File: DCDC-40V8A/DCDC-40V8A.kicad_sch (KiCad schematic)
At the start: 0 parts

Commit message: wip
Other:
- added sheet ADC-Coprocessor (adc_coprocessor.kicad_sch)
- sheet Power ports: added EN; removed none
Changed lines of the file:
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@@
 	(generator_version "9.0")
 	(paper "A4")
+	(junction
+		(at 104.14 52.07)
+		(diameter 0)
+		(color 0 0 0 0)
+	)
 	(bus
 		(pts
-			(xy 88.9 52.07) (xy 118.11 52.07)
+			(xy 88.9 52.07) (xy 104.14 52.07)
+		)
+		(stroke
+			(width 0)
+			(type default)
+		)
+	)
+	(bus
+		(pts
+			(xy 104.14 52.07) (xy 118.11 52.07)
 		)
 		(stroke
@@
 		(pts
 			(xy 88.9 54.61) (xy 118.11 54.61)
+		)
+		(stroke
+			(width 0)
+			(type default)
+		)
+	)
+	(bus
+		(pts
+			(xy 104.14 52.07) (xy 104.14 120.65)
 		)
 		(stroke
@@
 	)
 	(sheet
-		(at 118.11 30.48)
-		(size 48.26 106.68)
+		(at 49.53 120.65)
+		(size 118.11 31.75)
 		(exclude_from_sim no)
 		(in_bom yes)
@@
 			(color 0 0 0 0.0000)
 		)
+		(property "Sheetname" "ADC-Coprocessor"
+			(at 49.53 119.9384 0)
+			(effects
+				(font
+					(size 1.27 1.27)
+				)
+				(justify left bottom)
+			)
+		)
+		(property "Sheetfile" "adc_coprocessor.kicad_sch"
+			(at 49.53 152.9846 0)
+			(effects
+				(font
+					(size 1.27 1.27)
+				)
+				(justify left top)
+			)
+		)
+		(pin "I2C" bidirectional
+			(at 104.14 120.65 90)
+			(effects
+				(font
+					(size 1.27 1.27)
+				)
+				(justify right)
+			)
+		)
+		(instances
+			(project "DCDC-40V8A"
+				(path "/c2f330be-6ca8-4ed0-86db-c2e1bfb68425"
+					(page "4")
+				)
+			)
+		)
+	)
+	(sheet
+		(at 118.11 30.48)
+		(size 48.26 69.85)
+		(exclude_from_sim no)
+		(in_bom yes)
+		(on_board yes)
+		(dnp no)
+		(fields_autoplaced yes)
+		(stroke
+			(width 0.1524)
+			(type solid)
+		)
+		(fill
+			(color 0 0 0 0.0000)
+		)
 		(property "Sheetname" "Control-Connector"
 			(at 118.11 29.7684 0)
@@
 		)
 		(property "Sheetfile" "control_connector.kicad_sch"
-			(at 118.11 137.7446 0)
+			(at 118.11 100.9146 0)
 			(effects
 				(font
@@
 		)
 		(pin "Left_RX" input
-			(at 118.11 110.49 180)
+			(at 118.11 91.44 180)
 			(effects
 				(font
@@
 		)
 		(pin "Left_TX" output
-			(at 118.11 113.03 180)
+			(at 118.11 93.98 180)
 			(effects
 				(font
@@
 		)
 		(pin "Right_RX" input
-			(at 166.37 113.03 0)
+			(at 166.37 93.98 0)
 			(effects
 				(font
@@
 		)
 		(pin "Right_TX" output
-			(at 166.37 110.49 0)
+			(at 166.37 91.44 0)
 			(effects
 				(font
@@
 			)
 		)
+		(pin "EN" input
+			(at 76.2 99.06 270)
+			(effects
+				(font
+					(size 1.27 1.27)
+				)
+				(justify left)
+			)
+		)

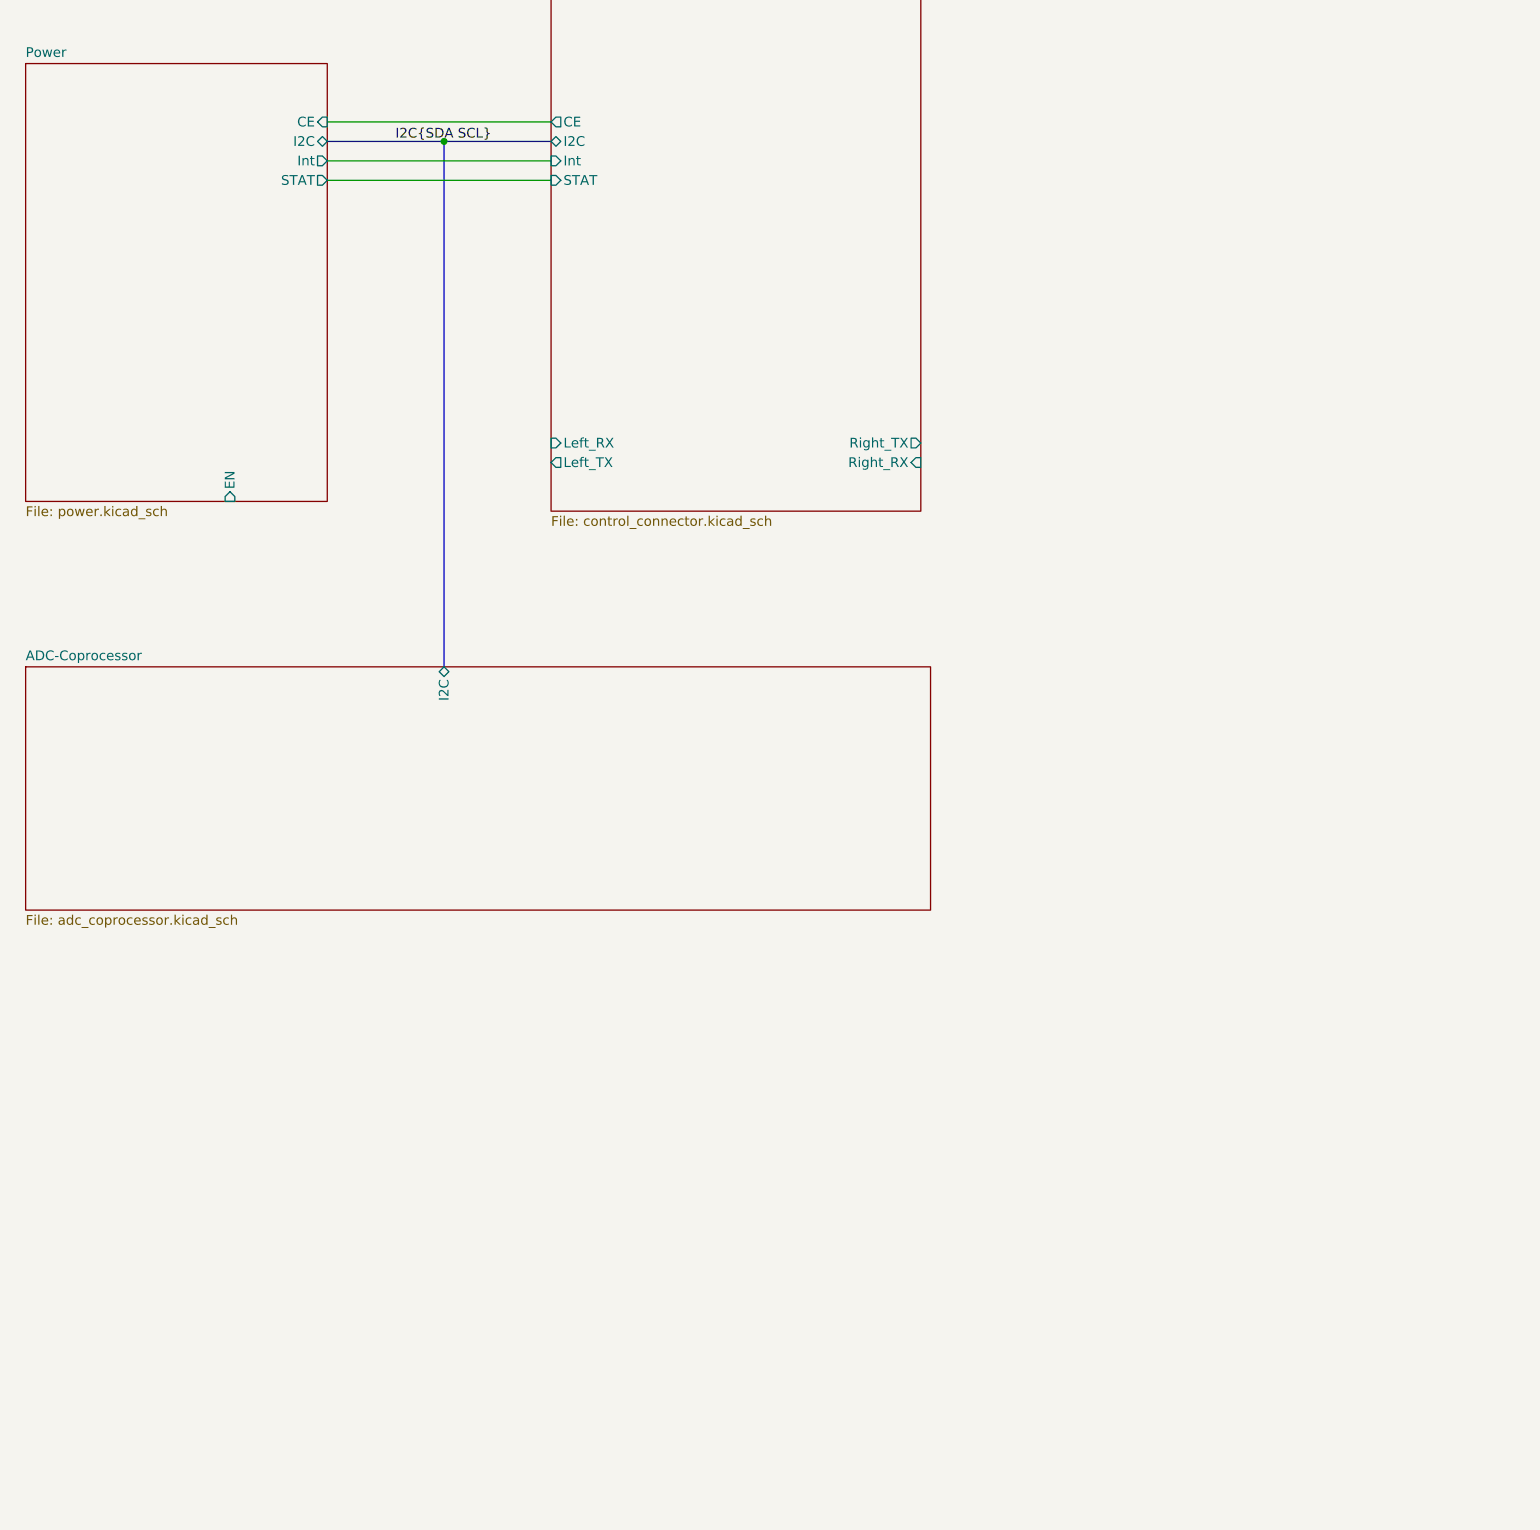
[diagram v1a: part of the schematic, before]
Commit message: move adc MUX and discharge to new sheet
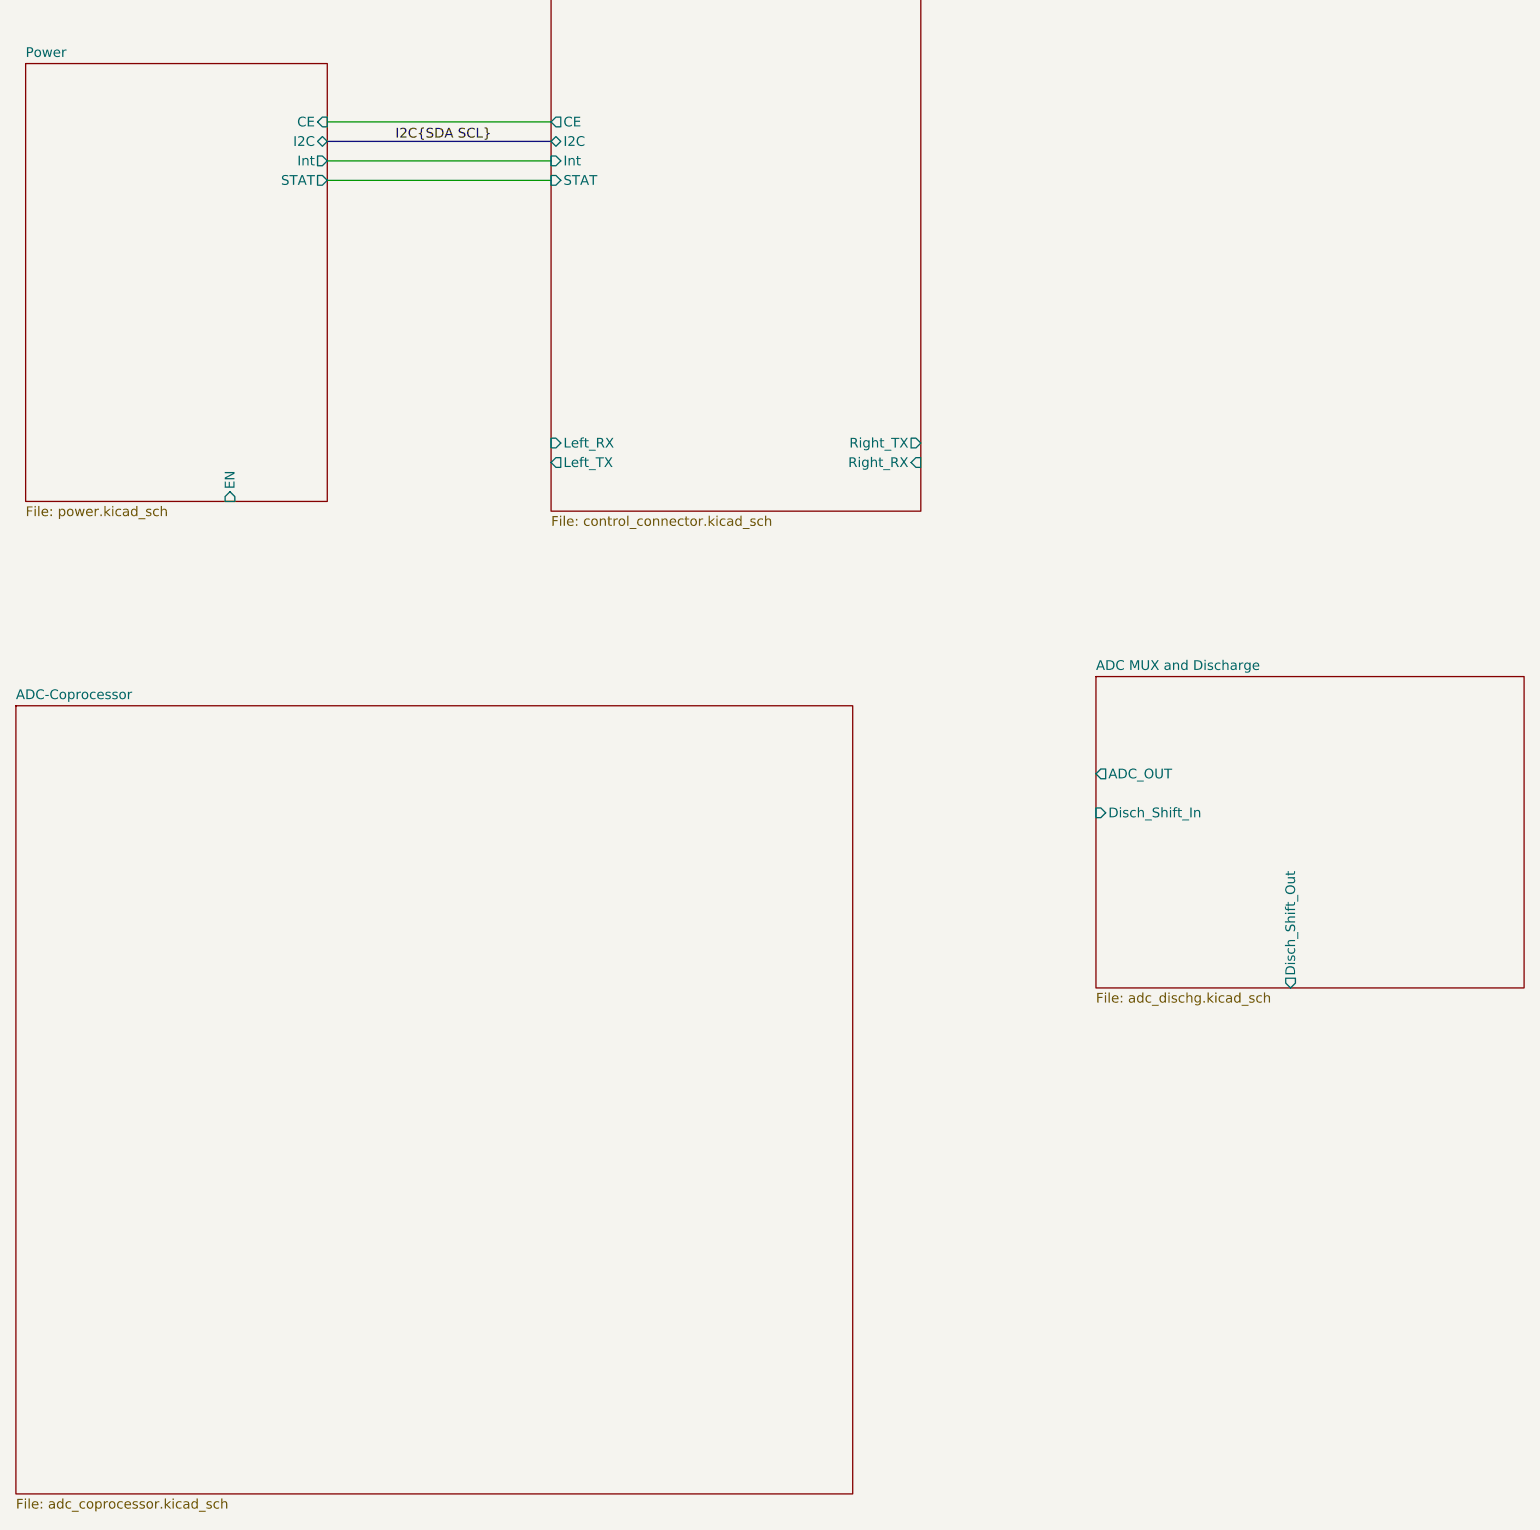
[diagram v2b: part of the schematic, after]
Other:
- added sheet ADC MUX and Discharge (adc_dischg.kicad_sch)
- sheet ADC-Coprocessor ports: added none; removed I2C
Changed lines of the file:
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@@
 (kicad_sch
-	(version 20250114)
+	(version 20260306)
 	(generator "eeschema")
-	(generator_version "9.0")
-	(paper "A4")
-	(junction
-		(at 104.14 52.07)
-		(diameter 0)
-		(color 0 0 0 0)
-	)
+	(generator_version "10.0")
+	(paper "A3")
 	(bus
 		(pts
-			(xy 88.9 52.07) (xy 104.14 52.07)
-		)
-		(stroke
-			(width 0)
-			(type default)
-		)
-	)
-	(bus
-		(pts
-			(xy 104.14 52.07) (xy 118.11 52.07)
+			(xy 88.9 52.07) (xy 118.11 52.07)
 		)
 		(stroke
@@
 		(pts
 			(xy 88.9 54.61) (xy 118.11 54.61)
-		)
-		(stroke
-			(width 0)
-			(type default)
-		)
-	)
-	(bus
-		(pts
-			(xy 104.14 52.07) (xy 104.14 120.65)
 		)
 		(stroke
@@
 	)
 	(sheet
-		(at 49.53 120.65)
-		(size 118.11 31.75)
+		(at 48.26 125.73)
+		(size 109.22 102.87)
 		(exclude_from_sim no)
 		(in_bom yes)
@@
 		)
 		(fill
-			(color 0 0 0 0.0000)
+			(color 0 0 0 0)
 		)
 		(property "Sheetname" "ADC-Coprocessor"
-			(at 49.53 119.9384 0)
+			(at 48.26 125.0184 0)
+			(show_name no)
+			(do_not_autoplace no)
 			(effects
 				(font
@@
 		)
 		(property "Sheetfile" "adc_coprocessor.kicad_sch"
-			(at 49.53 152.9846 0)
+			(at 48.26 229.1846 0)
+			(show_name no)
+			(do_not_autoplace no)
 			(effects
 				(font
@@
 				)
 				(justify left top)
-			)
-		)
-		(pin "I2C" bidirectional
-			(at 104.14 120.65 90)
-			(effects
-				(font
-					(size 1.27 1.27)
-				)
-				(justify right)
 			)
 		)
@@
 				(path "/c2f330be-6ca8-4ed0-86db-c2e1bfb68425"
 					(page "4")
+				)
+			)
+		)
+	)
+	(sheet
+		(at 189.23 121.92)
+		(size 55.88 40.64)
+		(exclude_from_sim no)
+		(in_bom yes)
+		(on_board yes)
+		(dnp no)
+		(fields_autoplaced yes)
+		(stroke
+			(width 0.1524)
+			(type solid)
+		)
+		(fill
+			(color 0 0 0 0)
+		)
+		(property "Sheetname" "ADC MUX and Discharge"
+			(at 189.23 121.2084 0)
+			(show_name no)
+			(do_not_autoplace no)
+			(effects
+				(font
+					(size 1.27 1.27)
+				)
+				(justify left bottom)
+			)
+		)
+		(property "Sheetfile" "adc_dischg.kicad_sch"
+			(at 189.23 163.1446 0)
+			(show_name no)
+			(do_not_autoplace no)
+			(effects
+				(font
+					(size 1.27 1.27)
+				)
+				(justify left top)
+			)
+		)
+		(pin "ADC_OUT" output
+			(at 189.23 134.62 180)
+			(effects
+				(font
+					(size 1.27 1.27)
+				)
+				(justify left)
+			)
+		)
+		(pin "Disch_Shift_In" input
+			(at 189.23 139.7 180)
+			(effects
+				(font
+					(size 1.27 1.27)
+				)
+				(justify left)
+			)
+		)
+		(pin "Disch_Shift_Out" output
+			(at 214.63 162.56 270)
+			(effects
+				(font
+					(size 1.27 1.27)
+				)
+				(justify left)
+			)
+		)
+		(instances
+			(project "DCDC-40V8A"
+				(path "/c2f330be-6ca8-4ed0-86db-c2e1bfb68425"
+					(page "6")
 				)
 			)
@@
 		)
 		(fill
-			(color 0 0 0 0.0000)
+			(color 0 0 0 0)
 		)
 		(property "Sheetname" "Control-Connector"
 			(at 118.11 29.7684 0)
+			(show_name no)
+			(do_not_autoplace no)
 			(effects
 				(font
@@
 		(property "Sheetfile" "control_connector.kicad_sch"
 			(at 118.11 100.9146 0)
+			(show_name no)
+			(do_not_autoplace no)
 			(effects
 				(font
@@
 		)
 		(fill
-			(color 0 0 0 0.0000)
+			(color 0 0 0 0)
 		)
 		(property "Sheetname" "Power"
 			(at 49.53 41.1984 0)
+			(show_name no)
+			(do_not_autoplace no)
 			(effects
 				(font
@@
 		(property "Sheetfile" "power.kicad_sch"
 			(at 49.53 99.6446 0)
-			(effects
-				(font
+			(show_name no)
+			(do_not_autoplace no)
+			(effects
+				(font

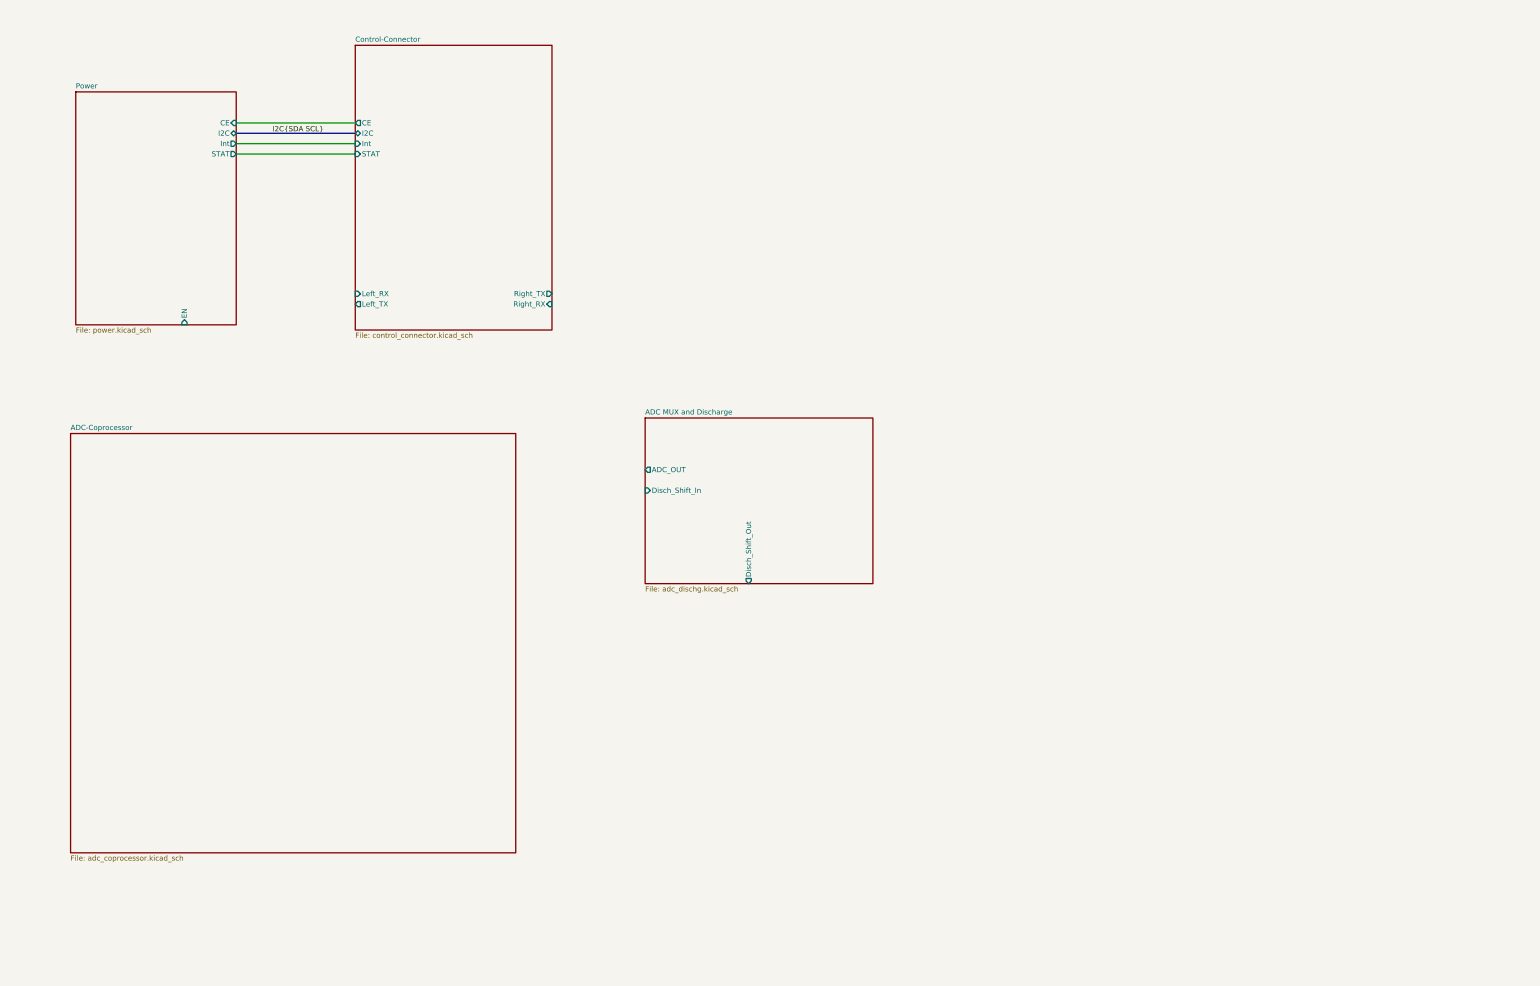
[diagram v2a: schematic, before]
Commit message: added discharge circuitry and help texts
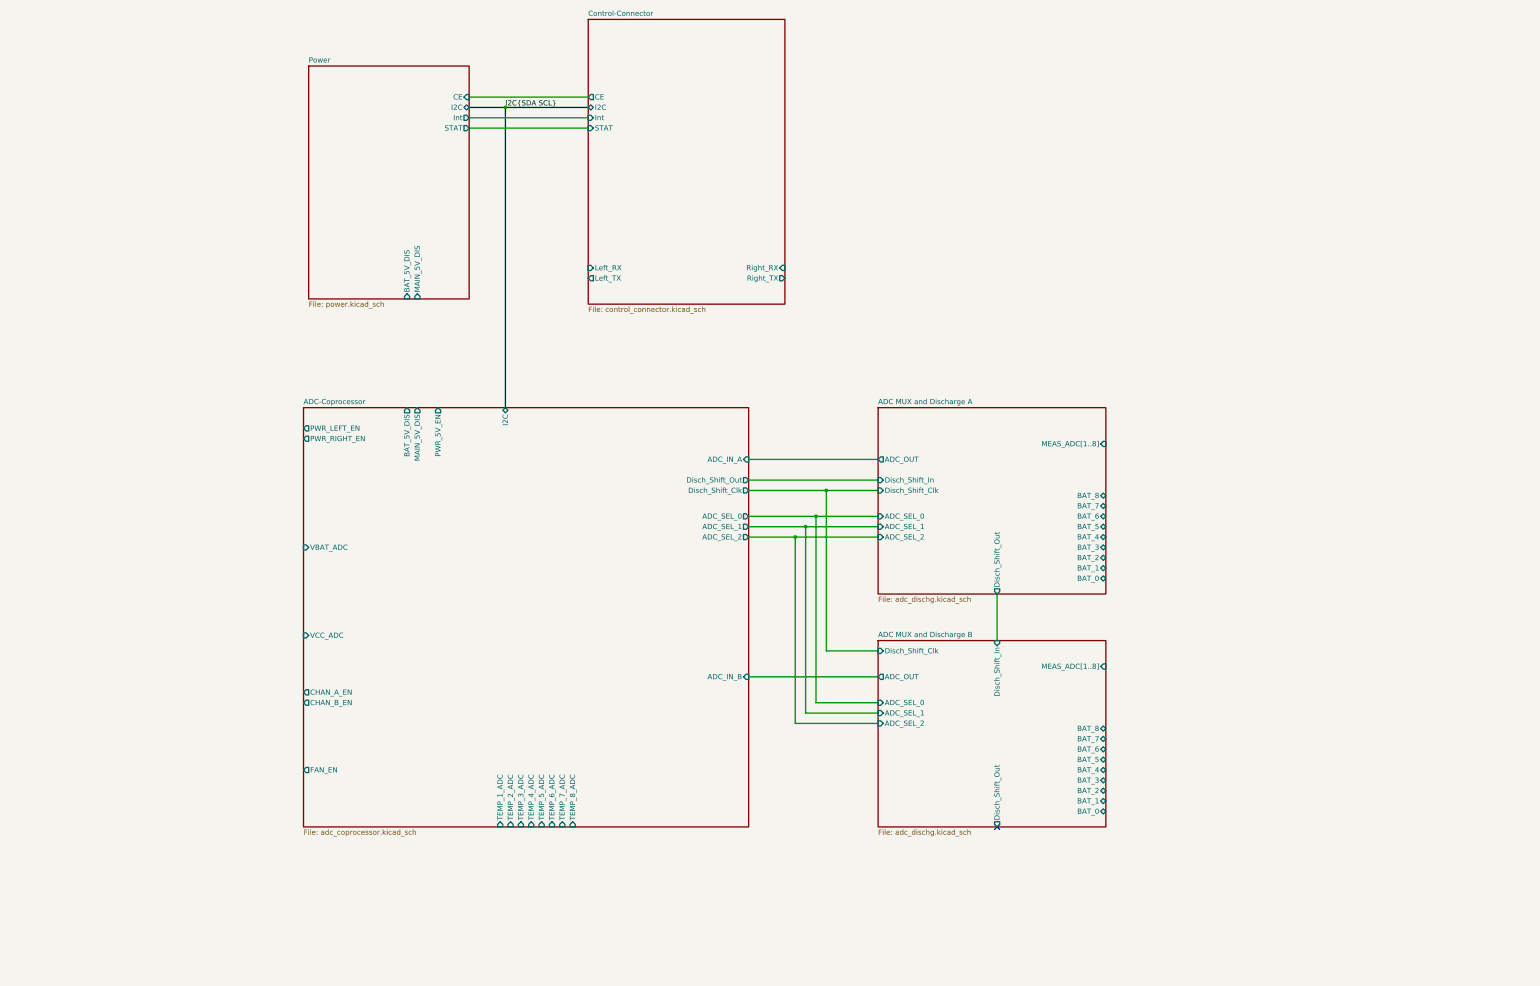
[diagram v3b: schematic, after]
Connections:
- no-connect marks 0 -> 1
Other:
- sheet ADC MUX and Discharge renamed ADC MUX and Discharge A
- added sheet ADC MUX and Discharge B (adc_dischg.kicad_sch)
- sheet ADC MUX and Discharge A ports: added ADC_SEL_0, ADC_SEL_1, ADC_SEL_2, BAT_0, BAT_1, BAT_2, BAT_3, BAT_4, BAT_5, BAT_6, BAT_7, BAT_8, Disch_Shift_Clk, MEAS_ADC[1..8]; removed none
- sheet ADC-Coprocessor ports: added ADC_IN_A, ADC_IN_B, ADC_SEL_0, ADC_SEL_1, ADC_SEL_2, BAT_5V_DIS, CHAN_A_EN, CHAN_B_EN, Disch_Shift_Clk, Disch_Shift_Out, FAN_EN, I2C, MAIN_5V_DIS, PWR_5V_EN, PWR_LEFT_EN, PWR_RIGHT_EN, TEMP_1_ADC, TEMP_2_ADC, TEMP_3_ADC, TEMP_4_ADC, TEMP_5_ADC, TEMP_6_ADC, TEMP_7_ADC, TEMP_8_ADC, VBAT_ADC, VCC_ADC; removed none
- sheet Power ports: added BAT_5V_DIS, MAIN_5V_DIS; removed EN
